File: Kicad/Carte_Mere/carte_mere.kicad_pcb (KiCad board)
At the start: 2 copper layers, 65 x 76 mm, 10 parts, among them J1 Alimentation, J3 HE10 (provenance)

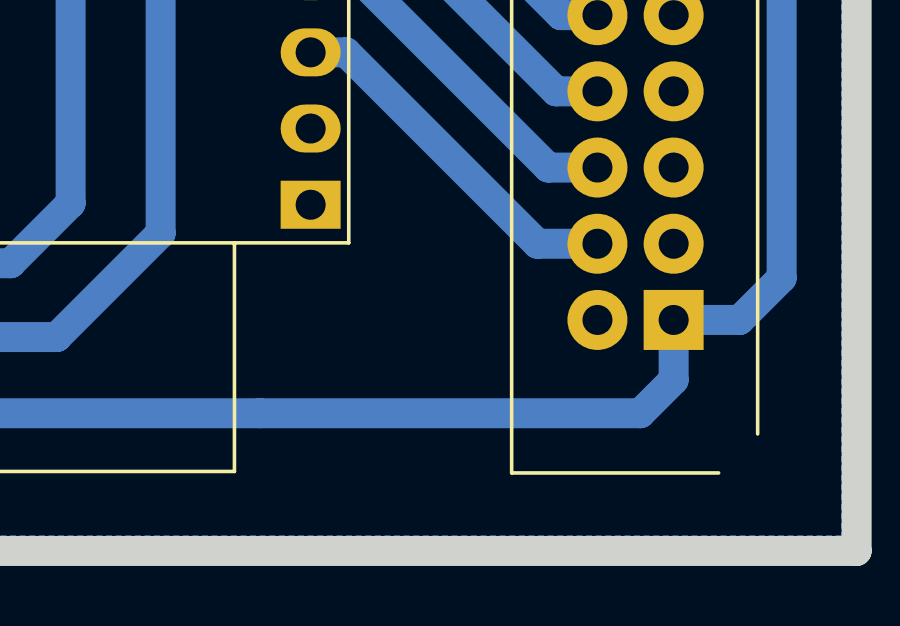
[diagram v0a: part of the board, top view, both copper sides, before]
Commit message: Ajout de code test bouton
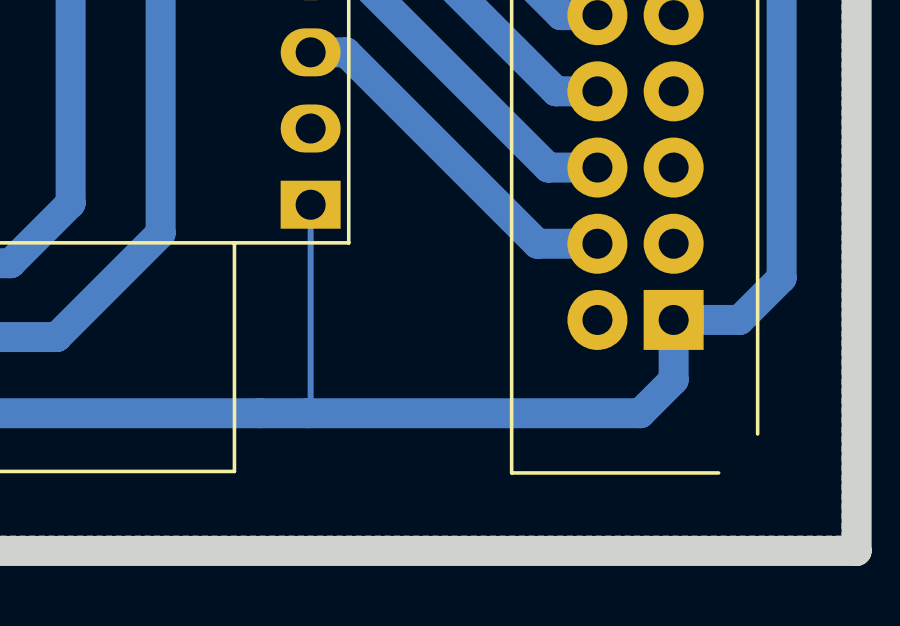
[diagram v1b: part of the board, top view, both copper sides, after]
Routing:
- net 3V3: track 192.4 -> 199.4 mm
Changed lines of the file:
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@@
+	)
+	(segment
+		(start 141 93.01)
+		(end 140.9 93.11)
+		(width 0.2)
+		(layer "B.Cu")
+		(net 3)
 	)
 	(segment
@@
 	)
 	(segment
+		(start 141 86.16)
+		(end 141 93.01)
+		(width 0.2)
+		(layer "B.Cu")
+		(net 3)
+	)
+	(segment
 		(start 151.99 93.11)
 		(end 153.1 92)
@@
 	)
 	(segment
-		(start 139.3 93.11)
+		(start 140.9 93.11)
 		(end 151.99 93.11)
 		(width 1)
@@
 		(width 1)
 		(layer "B.Cu")
+		(net 3)
+	)
+	(segment
+		(start 139.3 93.11)
+		(end 140.9 93.11)
+		(width 1)
+		(layer "B.Cu")
